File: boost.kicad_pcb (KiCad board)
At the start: 2 copper layers, 74 x 39 mm, 25 parts, among them J2 Conn_01x10_Pin, J3 Conn_01x10_Pin, Q1 G1003B-23, U2 LM3478MA

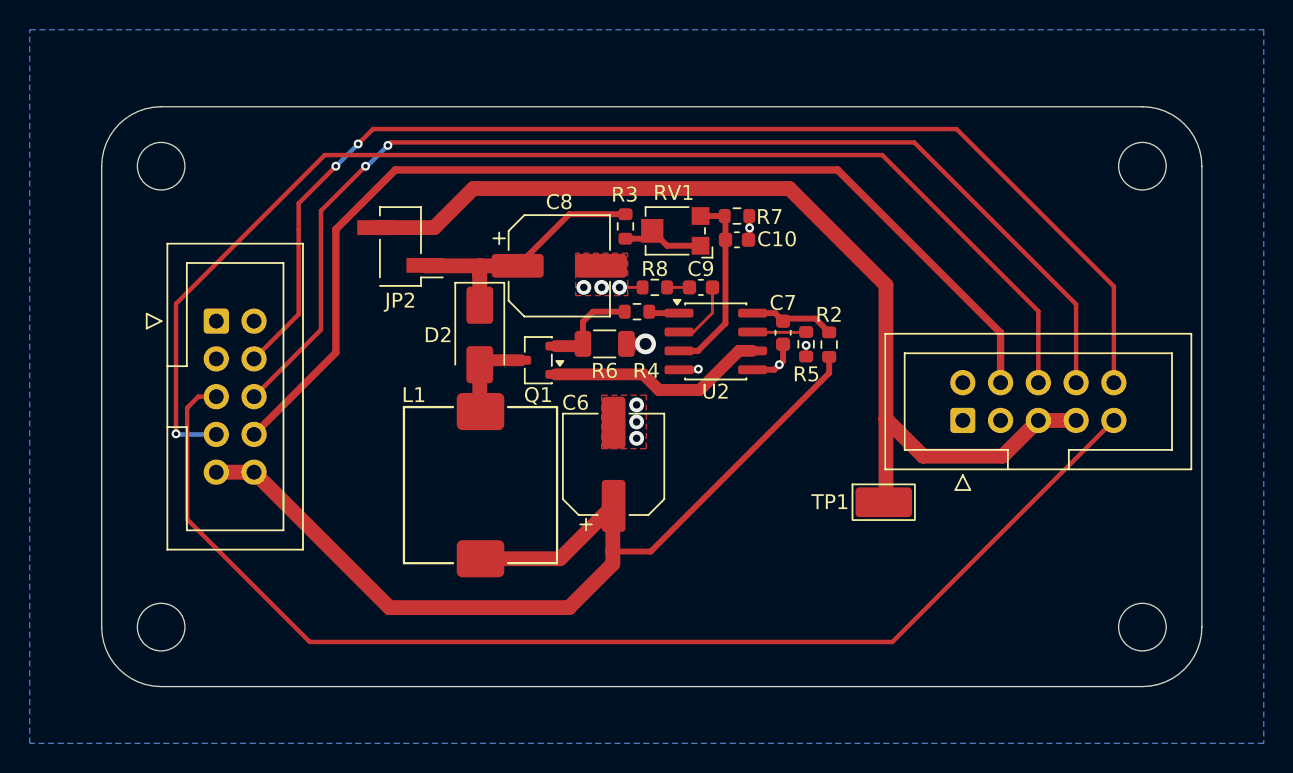
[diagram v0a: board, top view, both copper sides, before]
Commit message: Switched to breadboard formfactor
Also added files for GH
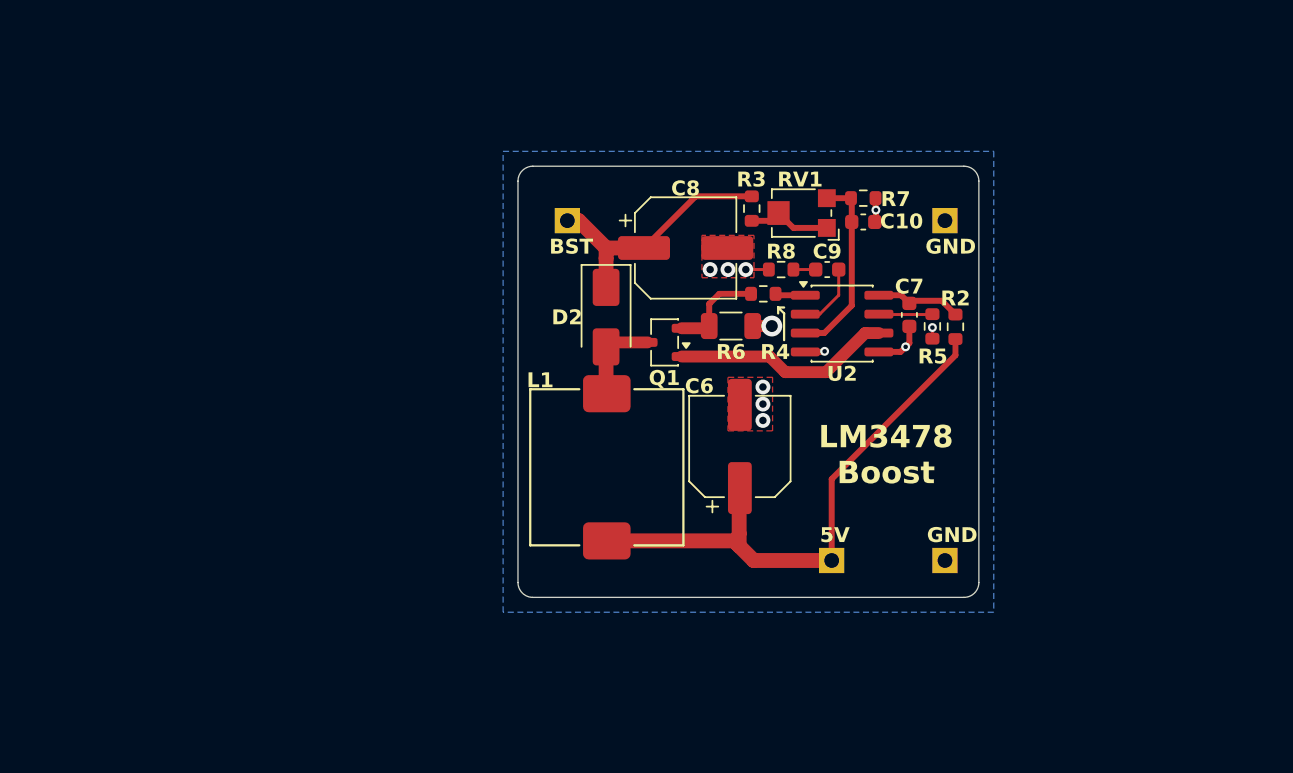
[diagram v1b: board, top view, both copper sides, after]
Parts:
- removed H1, H2, H3, H4: MountingHole, MountingHole:MountingHole_3.2mm_M3
- removed J2, J3: Conn_01x10_Pin, Connector_IDC:IDC-Header_2x05_P2.54mm_Vertical
- removed JP2: Jumper_2_Small_Bridged, Connector_PinHeader_2.54mm:PinHeader_1x02_P2.54mm_Vertical_SMD_Pin1Left
- removed TP1: TestPoint, CustomFootprints:TestPoint_Keystone_5019_Miniature
- added J1: Conn_01x01_Pin, Connector_PinHeader_2.54mm:PinHeader_1x01_P2.54mm_Vertical, B.Cu at (165.1, 96.5)
- added J4: Conn_01x01_Pin, Connector_PinHeader_2.54mm:PinHeader_1x01_P2.54mm_Vertical, B.Cu at (172.7, 73.7)
- added J5: Conn_01x01_Pin, Connector_PinHeader_2.54mm:PinHeader_1x01_P2.54mm_Vertical, B.Cu at (147.3, 73.7)
- added J6: Conn_01x01_Pin, Connector_PinHeader_2.54mm:PinHeader_1x01_P2.54mm_Vertical, B.Cu at (172.7, 96.5)
- moved C10 8.58 mm to (167.2, 73.8)
- moved C6 8.58 mm to (158.9, 88.8)
- moved C8 8.58 mm to (155.3, 75.5)
- moved C9 8.58 mm to (164.8, 77.0)
- moved L1 8.58 mm to (150.0, 90.2)
- moved Q1 8.58 mm to (153.9, 81.8)
- moved R2 8.58 mm to (173.4, 80.8)
- moved R3 8.58 mm to (159.7, 72.8)
- moved R4 8.58 mm to (160.5, 78.6)
- moved U2 8.58 mm to (165.8, 80.6)
- moved D2 8.58 mm to (149.9, 80.2)
- moved R5 8.58 mm to (171.9, 80.8)
- moved R7 8.58 mm to (167.2, 72.2)
- moved RV1 8.58 mm to (163.0, 73.2)
- moved C7 8.58 mm to (170.3, 80.0)
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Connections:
- net /50V_BOOST renamed +50V
- net VBUS renamed +5V
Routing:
- net SER: track 82.8 -> 0.00 mm, vias 1 -> 0
- net CLK: track 81.7 -> 0.00 mm
- net LATCH: track 79.5 -> 0.00 mm, vias 2 -> 0
- net OE: track 76.8 -> 0.00 mm, vias 2 -> 0
- net +3V3: track 70.3 -> 0.00 mm
- net 50V: track 67.6 -> 0.00 mm
- net +5V: track 66.6 -> 38.0 mm
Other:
- board size 74 x 39 mm -> 31 x 29 mm
- board text added: "5V"
- board text added: "BST"
- board text added: "GND"
- board text added: "LM3478 Boost"

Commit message: Added calculators
Changed component values to match calculator recommended values
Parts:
- C10: value 120p -> 100p
- C9: value 120p -> 82p
- R4: value 390 -> 422
- R6: value 150m -> 140m

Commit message: Changed to THT cap
Low ESR THT caps are easier to find. But I'm really changing cause the
SMD cap I wanted went out of stock :(
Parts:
- C6, C8: footprint Capacitor_SMD:CP_Elec_6.3x9.9 -> Capacitor_THT:CP_Radial_D6.3mm_P2.50mm
- moved C6 0.88 mm to (158.8, 88.0)
- moved C8 0.51 mm to (155.2, 75.0), turned to -90 degrees
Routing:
- net +5V: track 38.0 -> 39.1 mm
- net GND: track 9.76 -> 9.21 mm, vias 11 -> 6
- removed copper zone on F.Cu, net GND
